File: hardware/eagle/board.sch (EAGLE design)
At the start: 43 parts, among them IC1 TPS61165, IC2 TPS61165, Q1 12M, U1 24AA02, U2 24AA02E64T-I/OT, X1 MINI-USB-32005-301

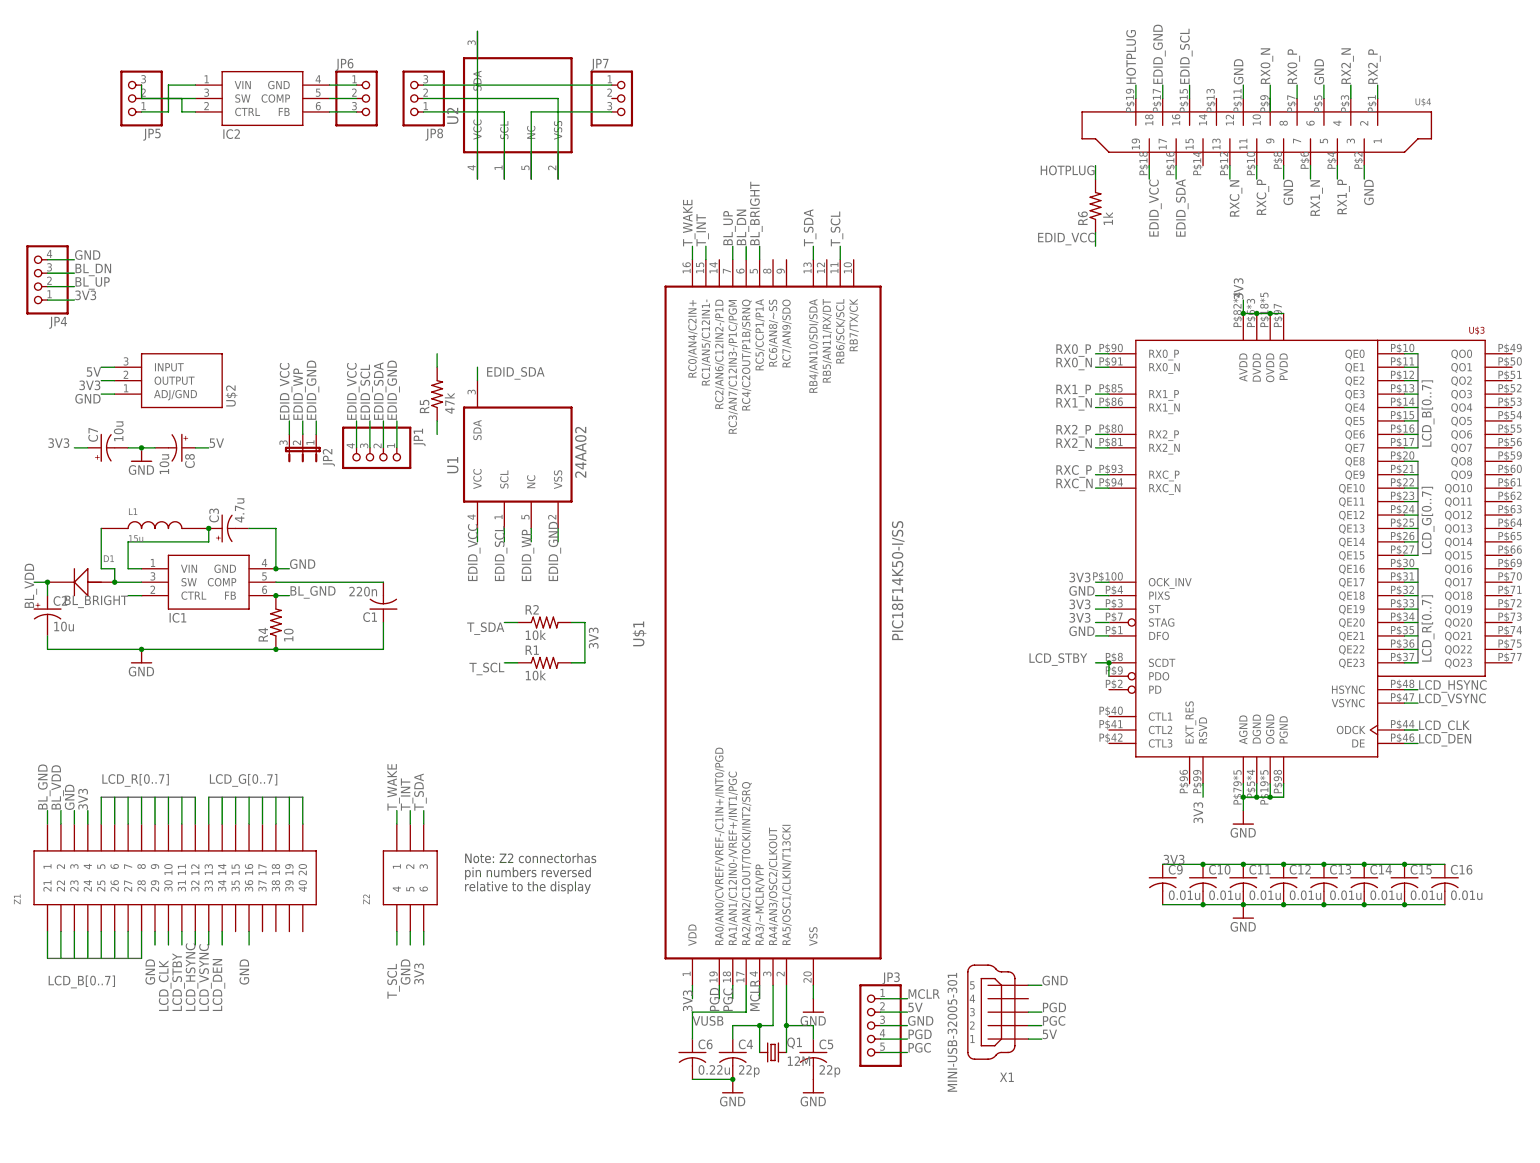
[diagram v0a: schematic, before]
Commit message: Update Eagle files
Tweaked design to shrink the PCB, remove
backlight buttons, and removed the diode
on MCLR for the microcontroller.
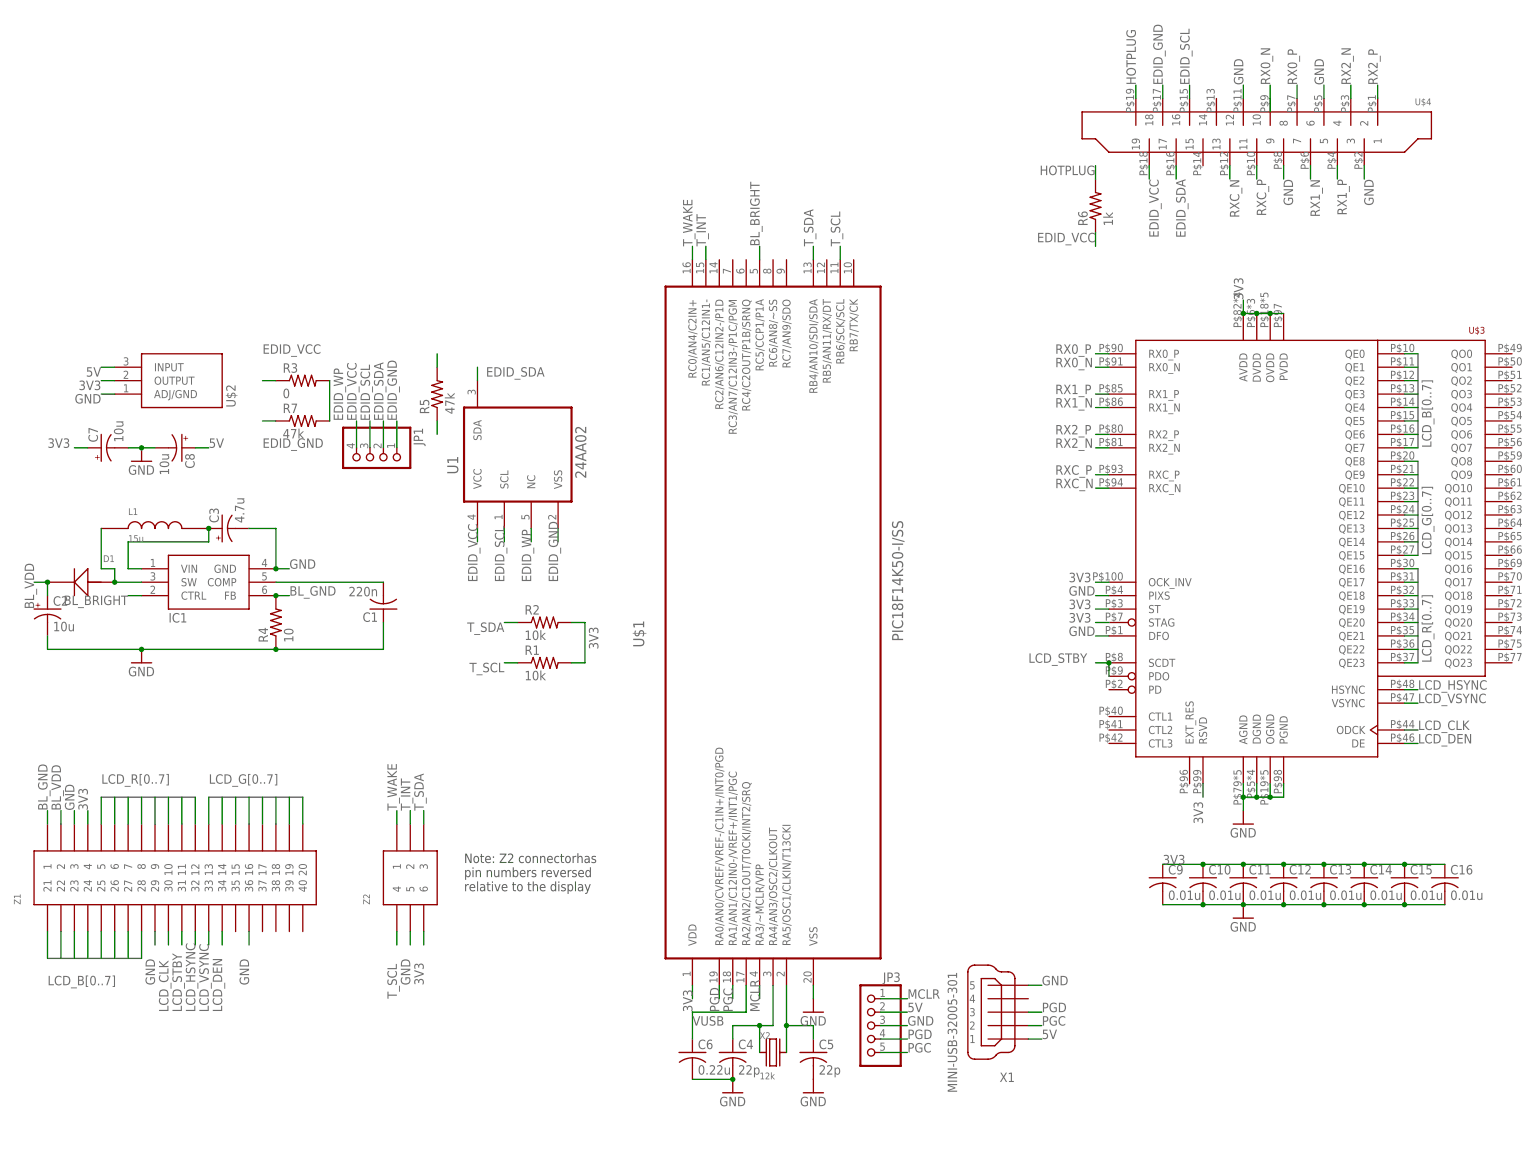
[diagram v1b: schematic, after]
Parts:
- removed IC2: TPS61165, ic:TPS61165
- removed JP2: (no value), jumper:JP2W
- removed JP4: (no value), pinhead:PINHD-1X4/90
- removed JP5, JP6, JP7, JP8: (no value), pinhead:PINHD-1X3
- removed Q1: 12M, crystal:CSM-7X-DU
- removed U2: 24AA02E64T-I/OT, Microchip-24AA02E64T-I_OT:24AA02E64T-I/OT
- added R3: 0, resistor:R-US_R0805
- added R7: 47k, resistor:R-US_R1206
- added X2: 12k, ic:CTS-445
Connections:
- removed net BL_DN: JP4.3, U$1.RC4/C2OUT/P1B/SRNQ
- removed net BL_UP: JP4.2, U$1.RC3/AN7/C12IN3-/P1C/PGM
- removed net N$10: JP8.2, U2.VSS
- removed net N$11: JP8.3, U2.SDA
- removed net N$12: JP7.1, U2.VCC
- removed net N$13: JP7.3, U2.NC
- removed net N$3: IC2.VIN, JP5.1
- removed net N$4: IC2.CTRL, JP5.2
- removed net N$5: IC2.SW, JP5.3
- removed net N$6: IC2.FB, JP6.3
- removed net N$7: IC2.COMP, JP6.2
- removed net N$8: IC2.GND, JP6.1
- removed net N$9: JP8.1, U2.SCL
- net 3V3: no longer JP4.1
- net EDID_GND: now also R7.1; no longer JP2.1
- net EDID_VCC: now also R3.1; no longer JP2.3
- net EDID_WP: now also R3.2, R7.2; no longer JP2.2
- net GND: no longer JP4.4
- net N$1: now also X2.P$1; no longer Q1.1
- net N$2: now also X2.P$2; no longer Q1.2
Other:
- note removed: "Backlight Buttons"

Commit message: Shrank circuit again.
Circuit board is smaller now, and also has the proper
wiring for low voltage programming. The missing resistor
was causing unexpected reboots of the device.
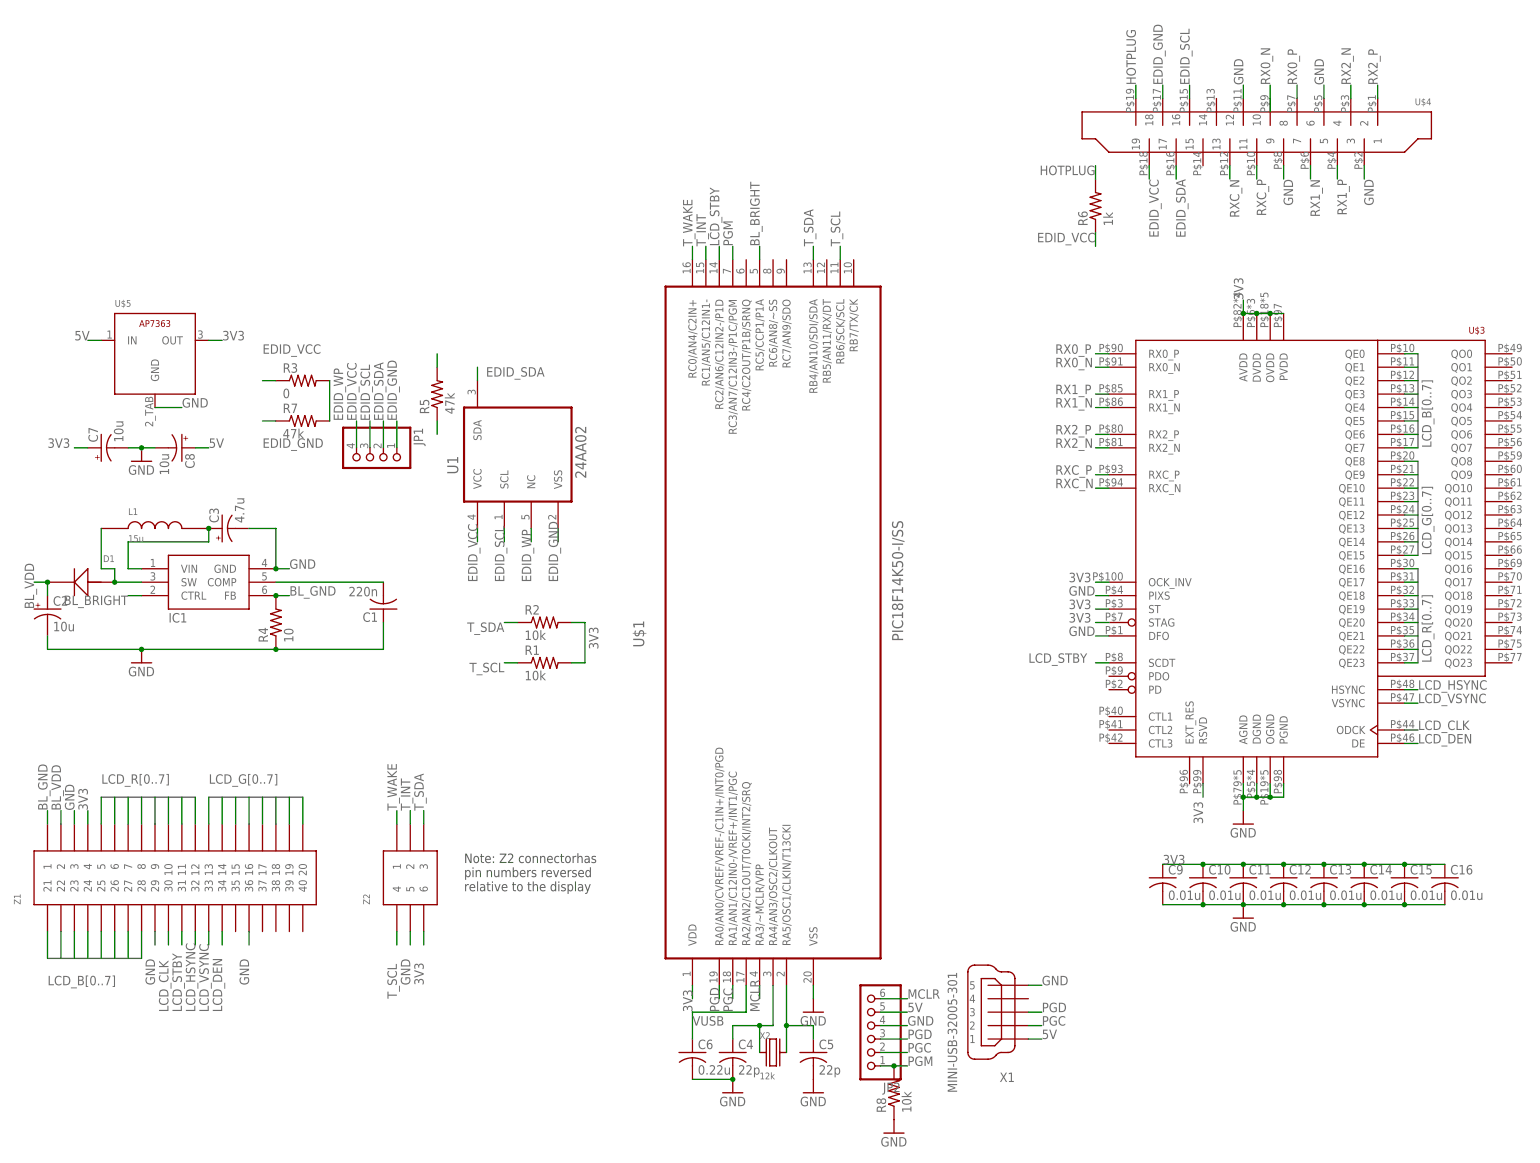
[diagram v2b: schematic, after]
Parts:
- removed JP3: (no value), pinhead:PINHD-1X5/90
- removed U$2: LM1086, lm1086:LM1086
- added JP2: (no value), pinhead:PINHD-1X6
- added R8: 10k, resistor:R-US_R1206
- added U$5: AP7363TO252, ap7363:AP7363TO252
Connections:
- new net PGM: JP2.1, R8.2, U$1.RC3/AN7/C12IN3-/P1C/PGM
- net 3V3: now also U$5.OUT; no longer U$2.OUTPUT
- net 5V: now also JP2.5, U$5.IN; no longer JP3.2, U$2.INPUT
- net GND: now also JP2.4, R8.1, U$5.GND; no longer JP3.3, U$2.ADJ/GND
- net LCD_STBY: now also U$1.RC2/AN6/C12IN2-/P1D; no longer U$3.PDO
- net MCLR: now also JP2.6; no longer JP3.1
- net PGC: now also JP2.2; no longer JP3.5
- net PGD: now also JP2.3; no longer JP3.4
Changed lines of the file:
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@@
 <part name="GND3" library="supply1" deviceset="GND" device=""/>
 <part name="C6" library="resistor" deviceset="C-US" device="C1206K" value="0.22u"/>
-<part name="JP3" library="pinhead" deviceset="PINHD-1X5" device="/90"/>
 <part name="X1" library="con-cypressindustries" deviceset="MINI-USB-" device="32005-301"/>
-<part name="U$2" library="lm1086" deviceset="LM1086" device=""/>
 <part name="C7" library="resistor" deviceset="CPOL-US" device="B" value="10u"/>
 <part name="C8" library="resistor" deviceset="CPOL-US" device="B" value="10u"/>
@@
 <part name="R7" library="resistor" deviceset="R-US_" device="R1206" value="47k"/>
 <part name="X2" library="ic" deviceset="CTS-445" device="" value="12k"/>
+<part name="JP2" library="pinhead" deviceset="PINHD-1X6" device=""/>
+<part name="R8" library="resistor" deviceset="R-US_" device="R1206" value="10k"/>
+<part name="GND7" library="supply1" deviceset="GND" device=""/>
+<part name="U$5" library="ap7363" deviceset="AP7363" device="TO252"/>
 </parts>
 <sheets>
@@
 <wire x1="50.8" y1="134.62" x2="50.8" y2="109.22" width="0.1524" layer="98"/>
 <text x="78.74" y="132.08" size="1.778" layer="98">EDID Memory</text>
-<wire x1="2.54" y1="134.62" x2="2.54" y2="109.22" width="0.1524" layer="98"/>
+<wire x1="2.54" y1="144.78" x2="2.54" y2="109.22" width="0.1524" layer="98"/>
 <wire x1="2.54" y1="109.22" x2="48.26" y2="109.22" width="0.1524" layer="98"/>
-<wire x1="48.26" y1="109.22" x2="48.26" y2="134.62" width="0.1524" layer="98"/>
-<wire x1="48.26" y1="134.62" x2="2.54" y2="134.62" width="0.1524" layer="98"/>
-<text x="5.08" y="132.08" size="1.778" layer="98">Main Power</text>
+<wire x1="48.26" y1="109.22" x2="48.26" y2="144.78" width="0.1524" layer="98"/>
+<wire x1="48.26" y1="144.78" x2="2.54" y2="144.78" width="0.1524" layer="98"/>
+<text x="5.08" y="142.24" size="1.778" layer="98">Main Power</text>
 </plain>
 <instances>
@@
 <instance part="GND3" gate="1" x="154.94" y="-7.62"/>
 <instance part="C6" gate="G$1" x="132.08" y="0"/>
-<instance part="JP3" gate="A" x="165.1" y="5.08" rot="MR0"/>
 <instance part="X1" gate="G$1" x="190.5" y="7.62" rot="R180"/>
-<instance part="U$2" gate="G$1" x="33.02" y="127" rot="R270"/>
 <instance part="C7" gate="G$1" x="20.32" y="114.3" rot="R90"/>
 <instance part="C8" gate="G$1" x="35.56" y="114.3" rot="R270"/>
@@
 <instance part="R7" gate="G$1" x="58.42" y="119.38"/>
 <instance part="X2" gate="G$1" x="147.32" y="0"/>
+<instance part="JP2" gate="A" x="165.1" y="5.08" rot="R180"/>
+<instance part="R8" gate="G$1" x="170.18" y="-7.62" rot="R90"/>
+<instance part="GND7" gate="1" x="170.18" y="-15.24"/>
+<instance part="U$5" gate="IC1" x="30.48" y="129.54"/>
 </instances>
 <busses>
@@
 </segment>
 <segment>
-<pinref part="JP3" gate="A" pin="3"/>
 <wire x1="172.72" y1="5.08" x2="167.64" y2="5.08" width="0.1524" layer="91"/>
 <label x="172.72" y="5.08" size="1.778" layer="95"/>
+<pinref part="JP2" gate="A" pin="4"/>
 </segment>
 <segment>
@@
 <wire x1="198.12" y1="12.7" x2="195.58" y2="12.7" width="0.1524" layer="91"/>
 <label x="198.12" y="12.7" size="1.778" layer="95"/>
-</segment>
-<segment>
-<pinref part="U$2" gate="G$1" pin="ADJ/GND"/>
-<wire x1="20.32" y1="124.46" x2="22.86" y2="124.46" width="0.1524" layer="91"/>
-<label x="20.32" y="124.46" size="1.778" layer="95" rot="R180"/>
 </segment>
 <segment>
@@
 <pinref part="GND6" gate="1" pin="GND"/>
 </segment>
+<segment>
+<pinref part="R8" gate="G$1" pin="1"/>
+<pinref part="GND7" gate="1" pin="GND"/>
+</segment>
+<segment>
+<pinref part="U$5" gate="IC1" pin="GND"/>
+<wire x1="30.48" y1="121.92" x2="35.56" y2="121.92" width="0.1524" layer="91"/>
+<label x="35.56" y="121.92" size="1.778" layer="95"/>
+</segment>
 </net>
 <net name="3V3" class="0">
@@
 <wire x1="132.08" y1="10.16" x2="132.08" y2="12.7" width="0.1524" layer="91"/>
 <label x="132.08" y="7.62" size="1.778" layer="95" rot="R90"/>
-</segment>
-<segment>
-<pinref part="U$2" gate="G$1" pin="OUTPUT"/>
-<wire x1="20.32" y1="127" x2="22.86" y2="127" width="0.1524" layer="91"/>
-<label x="20.32" y="127" size="1.778" layer="95" rot="R180"/>
 </segment>
 <segment>
@@
 <label x="220.98" y="35.56" size="1.778" layer="95"/>
 </segment>
+<segment>
+<pinref part="U$5" gate="IC1" pin="OUT"/>
+<wire x1="43.18" y1="134.62" x2="40.64" y2="134.62" width="0.1524" layer="91"/>
+<label x="43.18" y="134.62" size="1.778" layer="95"/>
+</segment>
 </net>
 <net name="LCD_CLK" class="0">
@@
 <pinref part="U$3" gate="G$1" pin="SCDT"/>
 <wire x1="210.82" y1="73.66" x2="208.28" y2="73.66" width="0.1524" layer="91"/>
-<pinref part="U$3" gate="G$1" pin="PDO"/>
-<wire x1="210.82" y1="73.66" x2="210.82" y2="71.12" width="0.1524" layer="91"/>
-<junction x="210.82" y="73.66"/>
 <label x="195.58" y="73.66" size="1.778" layer="95"/>
+</segment>
+<segment>
+<pinref part="U$1" gate="A" pin="RC2/AN6/C12IN2-/P1D"/>
+<wire x1="137.16" y1="152.4" x2="137.16" y2="149.86" width="0.1524" layer="91"/>
+<label x="137.16" y="152.4" size="1.778" layer="95" rot="R90"/>
 </segment>
 </net>
@@
 </segment>
 <segment>
-<pinref part="JP3" gate="A" pin="4"/>
 <wire x1="172.72" y1="2.54" x2="167.64" y2="2.54" width="0.1524" layer="91"/>
 <label x="172.72" y="2.54" size="1.778" layer="95"/>
+<pinref part="JP2" gate="A" pin="3"/>
 </segment>
 <segment>
@@
 </segment>
 <segment>
-<pinref part="JP3" gate="A" pin="5"/>
 <wire x1="172.72" y1="0" x2="167.64" y2="0" width="0.1524" layer="91"/>
 <label x="172.72" y="0" size="1.778" layer="95"/>
+<pinref part="JP2" gate="A" pin="2"/>
 </segment>
 <segment>
@@
 </segment>
 <segment>
-<pinref part="JP3" gate="A" pin="1"/>
 <wire x1="167.64" y1="10.16" x2="172.72" y2="10.16" width="0.1524" layer="91"/>
 <label x="172.72" y="10.16" size="1.778" layer="95"/>
+<pinref part="JP2" gate="A" pin="6"/>
 </segment>
 </net>
@@
 </segment>
 <segment>
-<pinref part="JP3" gate="A" pin="2"/>
 <wire x1="172.72" y1="7.62" x2="167.64" y2="7.62" width="0.1524" layer="91"/>
 <label x="172.72" y="7.62" size="1.778" layer="95"/>
-</segment>
-<segment>
-<pinref part="U$2" gate="G$1" pin="INPUT"/>
-<wire x1="20.32" y1="129.54" x2="22.86" y2="129.54" width="0.1524" layer="91"/>
-<label x="20.32" y="129.54" size="1.778" layer="95" rot="R180"/>
+<pinref part="JP2" gate="A" pin="5"/>
 </segment>
 <segment>
@@
 <label x="40.64" y="114.3" size="1.778" layer="95"/>
 </segment>
+<segment>
+<pinref part="U$5" gate="IC1" pin="IN"/>
+<wire x1="17.78" y1="134.62" x2="20.32" y2="134.62" width="0.1524" layer="91"/>
+<label x="15.24" y="134.62" size="1.778" layer="95"/>
+</segment>
 </net>
 <net name="RX0_P" class="0">
@@
 </segment>
 </net>
+<net name="PGM" class="0">
+<segment>
+<pinref part="JP2" gate="A" pin="1"/>
+<wire x1="172.72" y1="-2.54" x2="170.18" y2="-2.54" width="0.1524" layer="91"/>
+<label x="172.72" y="-2.54" size="1.778" layer="95"/>
+<pinref part="R8" gate="G$1" pin="2"/>
+<wire x1="170.18" y1="-2.54" x2="167.64" y2="-2.54" width="0.1524" layer="91"/>
+<junction x="170.18" y="-2.54"/>
+</segment>
+<segment>
+<pinref part="U$1" gate="A" pin="RC3/AN7/C12IN3-/P1C/PGM"/>
+<wire x1="139.7" y1="152.4" x2="139.7" y2="149.86" width="0.1524" layer="91"/>
+<label x="139.7" y="152.4" size="1.778" layer="95" rot="R90"/>
+</segment>
+</net>
